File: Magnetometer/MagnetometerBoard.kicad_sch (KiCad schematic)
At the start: 5 parts, among them J1 Conn_01x04_Socket, J2 Conn_01x04_Socket

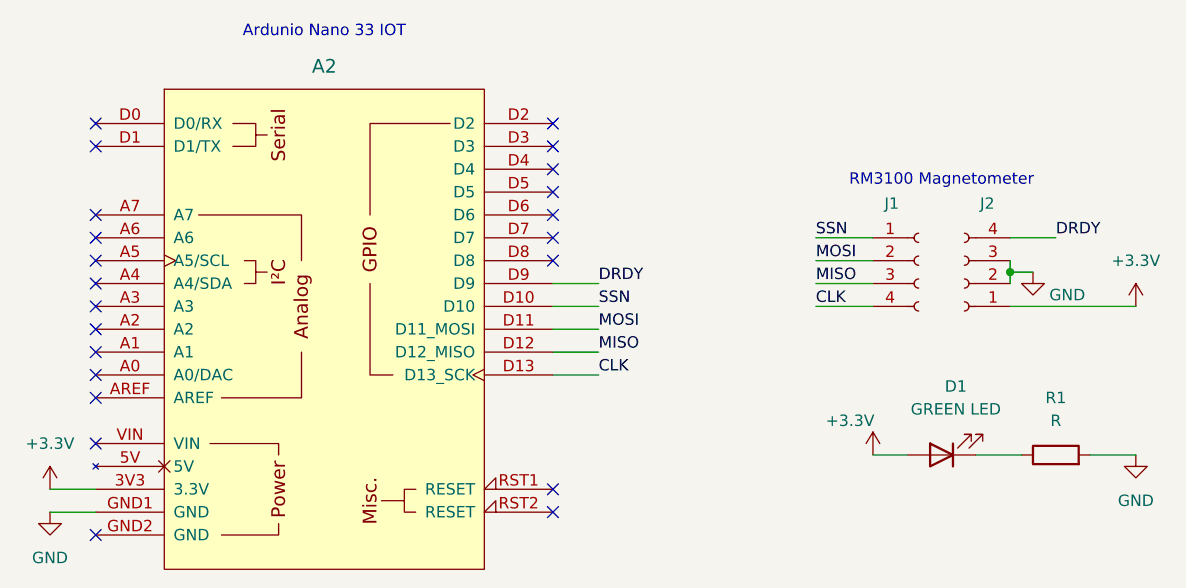
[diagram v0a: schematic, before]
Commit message: finailzied prototype for the magnetometer pcb
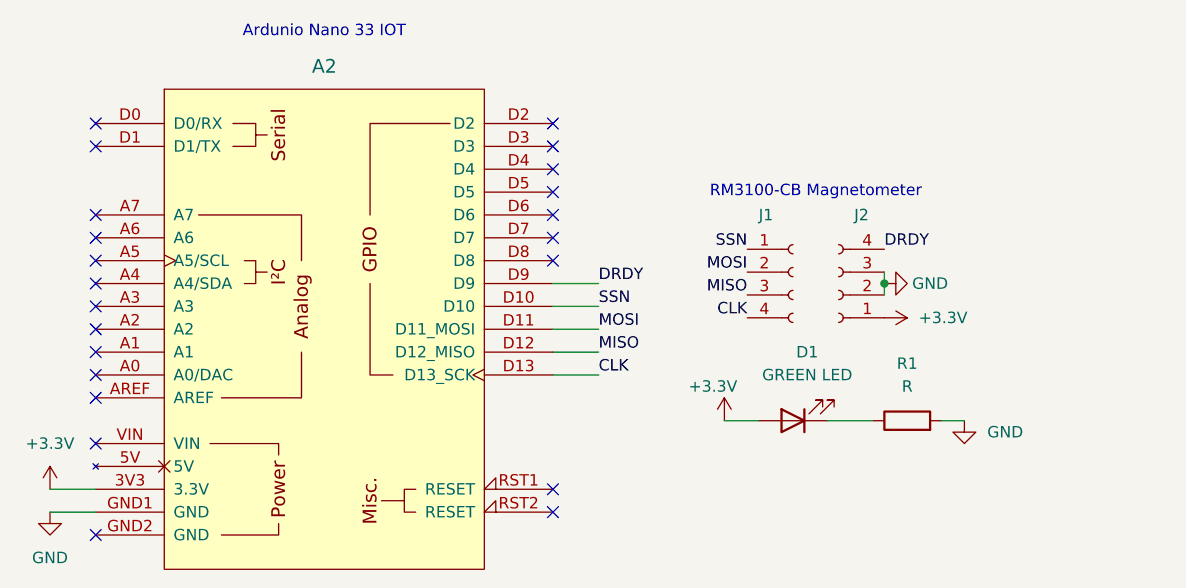
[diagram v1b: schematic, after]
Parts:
- D1: footprint (none) -> LED_THT:LED_D3.0mm
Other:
- note added: "RM3100-CB Magnetometer"
- note removed: "RM3100 Magnetometer"
- moved on the sheet: D1, J1, J2, R1
